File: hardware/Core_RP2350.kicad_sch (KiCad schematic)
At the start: 70 parts, among them SW1 SPST-NO, SW2 SPST-NO, SW3 SPST-NO, SW4 SPST-NO, SW5 SPST-NO, U1 RP2350B-QFN80, U2 LM4040A30IDBZR, U3 W25Q128JVS, U4 W25Q128JVS, U5 W25Q128JVS

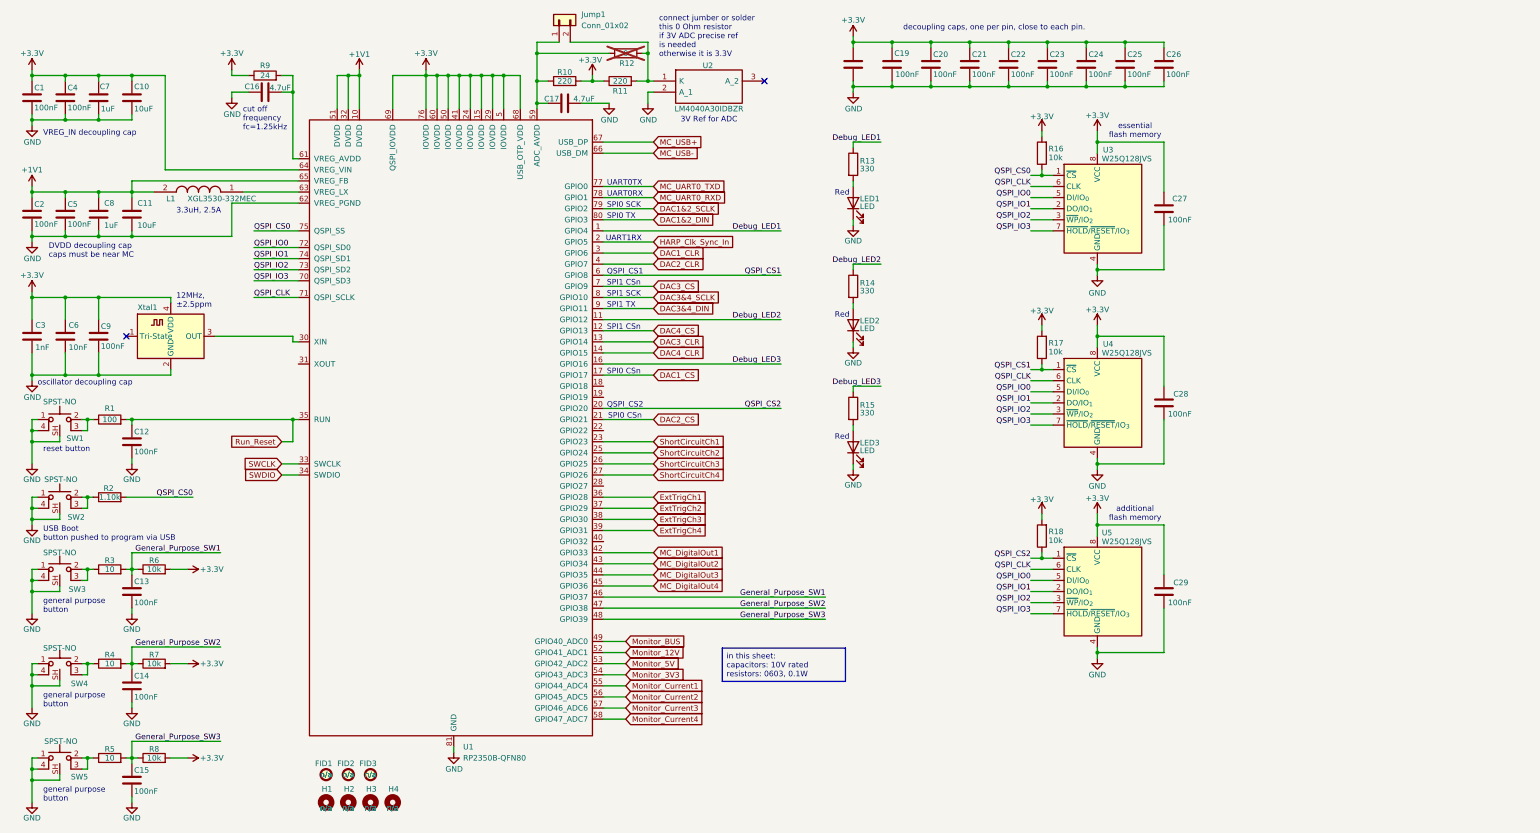
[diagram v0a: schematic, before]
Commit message: draft simplified rp2350 schematic w/sd card
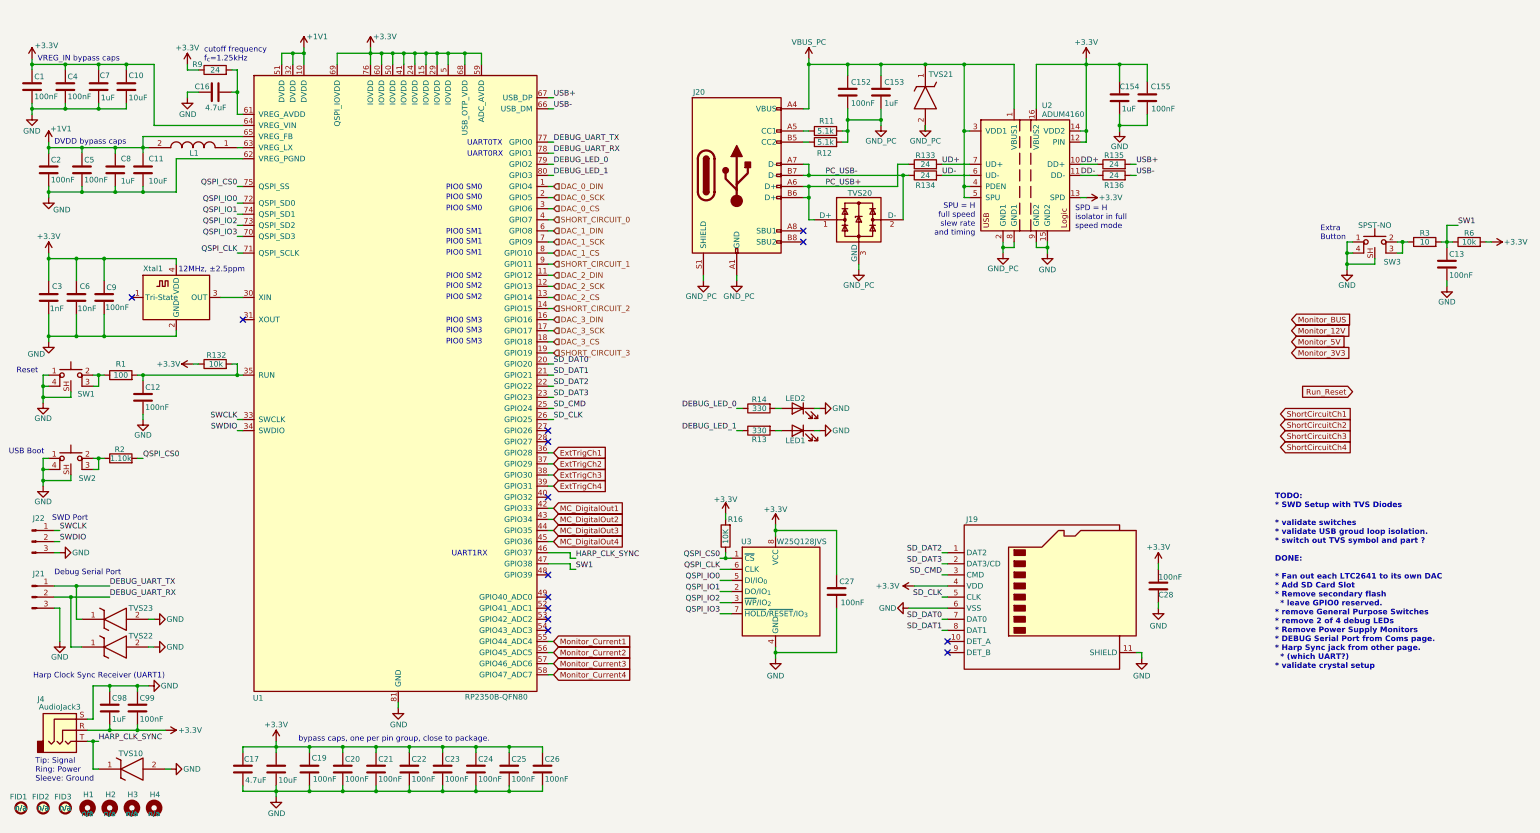
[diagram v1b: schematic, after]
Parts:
- removed C14, C15, C29: 100nF, Capacitor_SMD:C_0603_1608Metric, symbol harp.device.quad.dac:C_0603
- removed Jump1: Conn_01x02, Connector_PinHeader_2.54mm:PinHeader_1x02_P2.54mm_Vertical, symbol harp.device.quad.dac:Conn_01x02
- removed LED3: LED, harp.device.quad.dac.kicad:LED_0603_1608Metric_Pad1.05x0.95mm_HandSolder, symbol harp.device.quad.dac:LED
- removed R10: 220, Resistor_SMD:R_0603_1608Metric, symbol harp.device.quad.dac:R_0603
- removed R15: 330, Resistor_SMD:R_0603_1608Metric, symbol harp.device.quad.dac:R_0603
- removed R17, R18, R7, R8: 10k, Resistor_SMD:R_0603_1608Metric, symbol harp.device.quad.dac:R_0603
- removed R4, R5: 10, Resistor_SMD:R_0603_1608Metric, symbol harp.device.quad.dac:R_0603
- removed SW4, SW5: SPST-NO, harp.device.quad.dac.kicad:SW_Push_1P1T-SH_NO_Vertical_Wuerth_WS-TASV, symbol harp.device.quad.dac:SW_Push_with_gnd
- removed U2: LM4040A30IDBZR, harp.device.quad.dac.kicad:SOT95P237X112-3N, symbol harp.device.quad.dac:LM4040A30IDBZR
- removed U4, U5: W25Q128JVS, harp.device.quad.dac.kicad:SOIC-8_5.3x5.3mm_P1.27mm, symbol harp.device.quad.dac:W25Q128JVS
- added C152, C155, C99: 100nF, Capacitor_SMD:C_0603_1608Metric, symbol harp.device.quad.dac:C_0603
- added C153, C154, C98: 1uF, Capacitor_SMD:C_0603_1608Metric, symbol harp.device.quad.dac:C_0603
- added J19: Micro_SD_Card_Det_Hirose_DM3AT, Connector_Card:microSD_HC_Hirose_DM3AT-SF-PEJM5, symbol Connector:Micro_SD_Card_Det_Hirose_DM3AT
- added J20: USB_C_Receptacle_USB2.0, harp.device.quad.dac.kicad:USB_C_Receptacle_JAE_DX07S016JA1R1500, symbol harp.device.quad.dac:USB_C_Receptacle_USB2.0
- added J21, J22: 5-146281-3, harp.device.quad.dac.kicad:PinHeader_1x03_P2.54mm_Vertical, symbol harp.device.quad.dac:Conn_01x03_Male
- added J4: AudioJack3, harp.device.quad.dac.kicad:Jack_3.5mm_CUI_SJ-3524-SMT_Horizontal, symbol harp.device.quad.dac:AudioJack3
- added R132: 10k, Resistor_SMD:R_0603_1608Metric, symbol harp.device.quad.dac:R_0603
- added R133, R134, R135, R136: 24, Resistor_SMD:R_0603_1608Metric, symbol harp.device.quad.dac:R_0603
- added TVS10, TVS21, TVS22, TVS23: ESD441DPLR, harp.device.quad.dac.kicad:ESD441DPLR, symbol harp.device.quad.dac:ESD441DPLR
- added TVS20: TPD2EUSB30, Package_TO_SOT_SMD:Texas_DRT-3, symbol harp.device.quad.dac:TPD2EUSB30
- added U2: ADUM4160, harp.device.quad.dac.kicad:SOIC-16W_7.5x10.3mm_P1.27mm, symbol harp.device.quad.dac:ADUM4160
- R11: value 220 -> 5.1k; Link https://www.digikey.com/en/products/detail/yageo/RC0603FR-07220RL/727061 -> https://www.digikey.com/en/products/detail/yageo/RC0603FR-075K1L/727268; Manufacturer Number RT0402BRD071KL -> RT0402FRE075K1L; Manufacturer_Part_Number RC0603FR-07220RL -> RC0603FR-075K1L; PCBWay Link (none) -> https://www.pcbway.com/components/detail/RT0402FRE075K1L/44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
- R12: value 0 -> 5.1k; Link https://www.digikey.com/en/products/detail/yageo/RC0603JR-0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 -> https://www.digikey.com/en/products/detail/yageo/RC0603FR-0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; Manufacturer Number RT0402BRD071KL -> RT0402FRE075K1L; Manufacturer_Part_Number RC0603JR-070RL -> RC0603FR-075K1L; PCBWay Link (none) -> https://www.pcbway.com/components/detail/RT0402FRE075K1L/44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; Tolerance (none) -> 1%; now fitted; now in the parts list
- R16: value 10k -> 10K
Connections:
- net General_Purpose_SW2 is gone; now on net SW1: U1.47 (GPIO38)
- net +3.3V: now also C17.1, C28.1, U1.59 (ADC_AVDD), C154.1, C155.2, C98.2, C99.1, J19.4 (VDD), J4.R, R132.1, U2.12 (PIN), U2.13 (SPD), U2.14 (VDD2), U2.16 (VBUS2); no longer C28.2, R11.1
- net GND: now also C28.2, C154.2, C155.1, C98.1, C99.2, J19.11 (SHIELD), J19.6 (VSS), J21.3 (Pin_3), J22.3 (Pin_3), J4.S, TVS10.2, TVS22.2, TVS23.2, U2.15 (GND2), U2.9 (GND2); no longer C28.1
- net Monitor_12V: no longer U1.52 (GPIO41_ADC1)
- net Monitor_3V3: no longer U1.54 (GPIO43_ADC3)
- net Monitor_5V: no longer U1.53 (GPIO42_ADC2)
- net Monitor_BUS: no longer U1.49 (GPIO40_ADC0)
- net Run_Reset: no longer C12.2, R1.2, U1.35 (RUN)
- net SWCLK: now also J22.1 (Pin_1)
- net SWDIO: now also J22.2 (Pin_2)
- net ShortCircuitCh1: no longer U1.23 (GPIO23)
- net ShortCircuitCh2: no longer U1.25 (GPIO24)
- net ShortCircuitCh3: no longer U1.26 (GPIO25)
- net ShortCircuitCh4: no longer U1.27 (GPIO26)
- net GND_PC: now reaches R11.2, R12.2
- net GND_PC: now also C152.1, C153.2, J20.A1 (GND), J20.A12 (GND), J20.B1 (GND), J20.B12 (GND), J20.S1 (SHIELD), TVS20.3 (GND), TVS21.2, U2.2 (GND1), U2.8 (GND1)
- net DAC_3_CS: now reaches U1.18 (GPIO18)
- net SHORT_CIRCUIT_3: now reaches U1.19 (GPIO19)
- net SD_DAT2: now reaches U1.22 (GPIO22)
- net SD_DAT2: now also J19.1 (DAT2)
- net DAC1&2_DIN renamed DEBUG_LED_1
- net DEBUG_LED_1: now also R13.1
- net DAC1&2_SCLK renamed DEBUG_LED_0
- net DEBUG_LED_0: now also R14.1
- net DAC1_CLR renamed DAC_0_CS
- net DAC1_CS renamed DAC_3_SCK
- net DAC2_CLR renamed SHORT_CIRCUIT_0
- net DAC2_CS renamed SD_DAT1
- net SD_DAT1: now also J19.8 (DAT1)
- net DAC3&4_DIN renamed SHORT_CIRCUIT_1
- net DAC3&4_SCLK renamed DAC_1_CS
- net DAC3_CLR renamed DAC_2_CS
- net DAC3_CS renamed DAC_1_SCK
- net DAC4_CLR renamed SHORT_CIRCUIT_2
- net DAC4_CS renamed DAC_2_SCK
- net Debug_LED1 renamed DAC_0_DIN
- net DAC_0_DIN: no longer R13.1
- net Debug_LED2 renamed DAC_2_DIN
- net DAC_2_DIN: no longer R14.1
- net Debug_LED3 renamed DAC_3_DIN
- net General_Purpose_SW1 renamed SW1
- net SW1: no longer U1.46 (GPIO37)
- net General_Purpose_SW3: no longer names the net of U1.48 (GPIO39)
- net HARP_Clk_Sync_In renamed DAC_0_SCK
- net MC_UART0_RXD renamed DEBUG_UART_RX
- net DEBUG_UART_RX: now also J21.2 (Pin_2), TVS22.1
- net MC_UART0_TXD renamed DEBUG_UART_TX
- net DEBUG_UART_TX: now also J21.1 (Pin_1), TVS23.1
- net MC_USB+ renamed USB+
- net USB+: now also R135.2
- net MC_USB- renamed USB-
- net USB-: now also R136.2
- net QSPI_CS1 renamed DAC_1_DIN
- net QSPI_CS2 renamed SD_DAT0
- net SD_DAT0: now also J19.7 (DAT0)
- new net: C12.2, R1.2, R132.2, U1.35 (RUN)
- new net: J20.A5 (CC1), R11.1
- new net: J20.B5 (CC2), R12.1
- new net DD+: R135.1, U2.10 (DD+)
- new net DD-: R136.1, U2.11 (DD-)
- new net HARP_CLK_SYNC: J4.T, TVS10.1, U1.46 (GPIO37)
- new net PC_USB+: J20.A6 (D+), J20.B6 (D+), R133.1, TVS20.1 (D+)
- new net PC_USB-: J20.A7 (D-), J20.B7 (D-), R134.1, TVS20.2 (D-)
- new net SD_CLK: J19.5 (CLK), U1.26 (GPIO25)
- new net SD_CMD: J19.3 (CMD), U1.25 (GPIO24)
- new net SD_DAT3: J19.2 (DAT3/CD), U1.23 (GPIO23)
- new net UD+: R133.2, U2.7 (UD+)
- new net UD-: R134.2, U2.6 (UD-)
- new net VBUS_PC: C152.2, C153.1, J20.A4 (VBUS), J20.A9 (VBUS), J20.B4 (VBUS), J20.B9 (VBUS), TVS21.1, U2.1 (VBUS1), U2.3 (VDD1), U2.4 (PDEN), U2.5 (SPU)
- no-connect marks 2 -> 14
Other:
- note added: "DVDD bypass caps"
- note added: "Debug Serial Port"
- note added: "Extra Button"
- note added: "Harp Clock Sync Receiver (UART1)"
- note added: "PIO0 SM0"
- note added: "PIO0 SM1"
- note added: "PIO0 SM2"
- note added: "PIO0 SM3"
- note added: "Reset"
- note added: "SPD = H isolator in full speed mode"
- note added: "SPU = H full speed slew rate and timing"
- note added: "SWD Port"
- note added: "TODO: * SWD Setup with TVS Diodes * validate switches * validate USB groud loop isolation. * switch out TVS symbol and part ? DONE: * Fan out each LTC2641 to its own DAC * Add SD Card Slot * Remove secondary flash * leave GPIO0 reserved. * remove General Purpose Switches * remove 2 of 4 debug LEDs * Remove Power Supply Monitors * DEBUG Serial Port from Coms page. * Harp Sync jack from other page.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"
- note added: "Tip: Signal Ring: Power Sleeve: Ground"
- note added: "USB Boot"
- note added: "VREG_IN bypass caps"
- note added: "bypass caps, one per pin group, close to package."
- note added: "cutoff frequency f_{c}=1.25kHz"
- note removed: "3.3uH, 2.5A"
- note removed: "3V Ref for ADC"
- note removed: "DVDD decoupling cap caps must be near MC"
- note removed: "QSPI_CS1"
- note removed: "QSPI_CS2"
- note removed: "Red"
- note removed: "SPI0 CSn"
- note removed: "SPI0 SCK"
- note removed: "SPI0 TX"
- note removed: "SPI1 CSn"
- note removed: "SPI1 SCK"
- note removed: "SPI1 TX"
- note removed: "USB Boot button pushed to program via USB"
- note removed: "VREG_IN decoupling cap"
- note removed: "additional flash memory"
- note removed: "connect jumber or solder this 0 Ohm resistor if 3V ADC precise ref is needed otherwise it is 3.3V"
- note removed: "cut off frequency fc=1.25kHz"
- note removed: "decoupling caps, one per pin, close to each pin."
- note removed: "essential flash memory"
- note removed: "general purpose button"
- note removed: "oscillator decoupling cap"
- note removed: "reset button"
- moved on the sheet: C1, C10, C11, C12, C13, C16, C17, C19, C2, C20, C21, C22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

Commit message: draft new analog signal chain & short-circuit detection
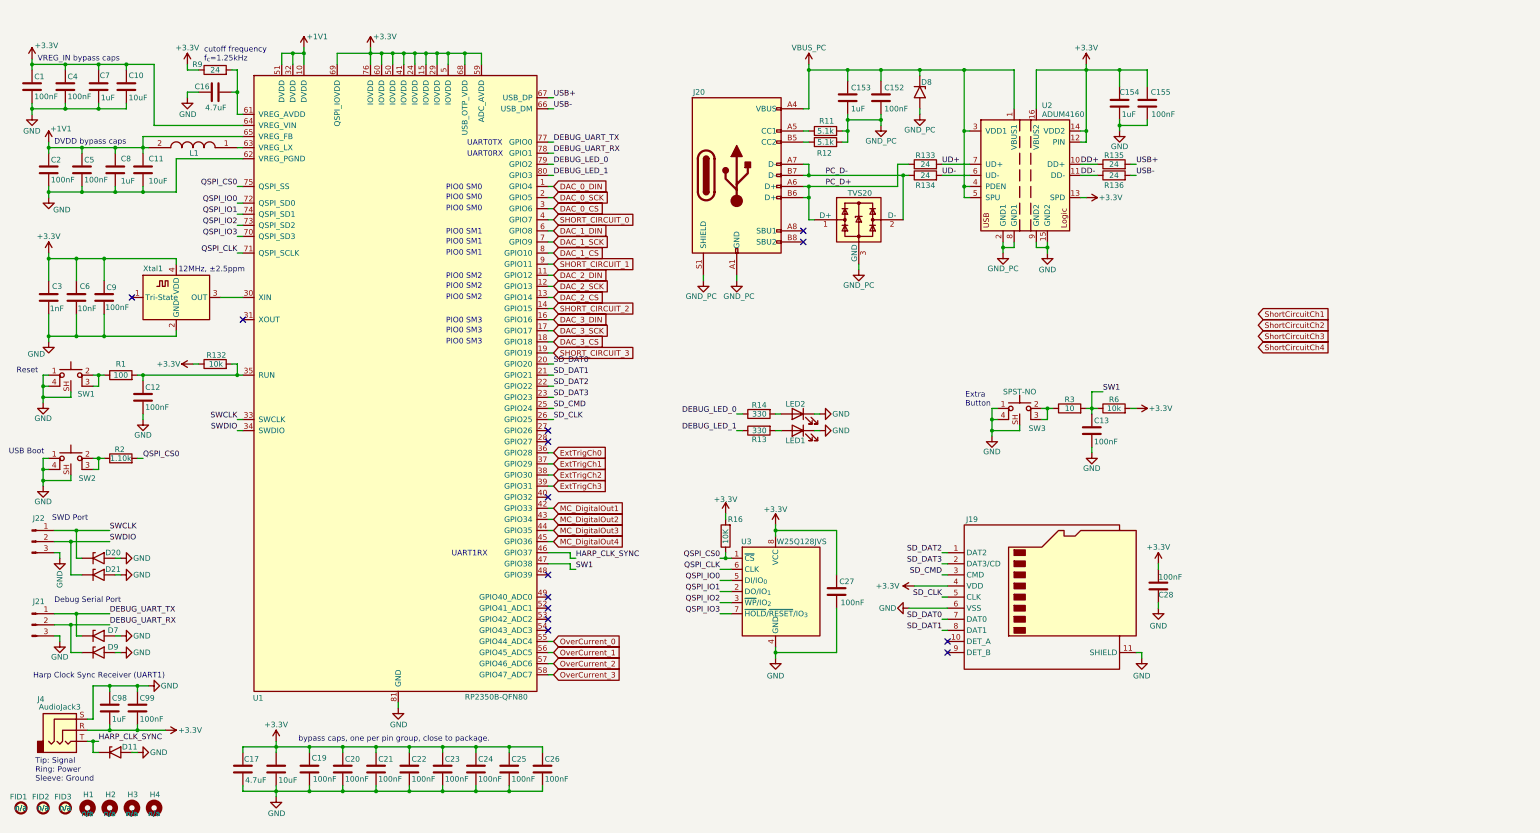
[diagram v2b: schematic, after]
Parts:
- removed TVS10, TVS21, TVS22, TVS23: ESD441DPLR, harp.device.quad.dac.kicad:ESD441DPLR, symbol harp.device.quad.dac:ESD441DPLR
- added D11, D20, D21, D7, D8, D9: VBUS05N1-HD1-G3-08, Diode_SMD:D_SOD-882, symbol kicad_component_library:VBUS05N1-HD1-G3-08
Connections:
- net ExtTrigCh4 is gone; now on net ExtTrigCh3: U1.39 (GPIO31)
- net DEBUG_UART_RX: now also D9.1 (A1)
- net DEBUG_UART_TX: now also D7.1 (A1)
- net ExtTrigCh1: now also U1.37 (GPIO29); no longer U1.36 (GPIO28)
- net ExtTrigCh2: now also U1.38 (GPIO30); no longer U1.37 (GPIO29)
- net ExtTrigCh3: no longer U1.38 (GPIO30)
- net GND: now also D11.2 (A2), D20.2 (A2), D21.2 (A2), D7.2 (A2), D9.2 (A2)
- net GND_PC: now also D8.2 (A2)
- net HARP_CLK_SYNC: now also D11.1 (A1)
- net SWCLK: now also D20.1 (A1)
- net SWDIO: now also D21.1 (A1)
- net VBUS_PC: now also D8.1 (A1)
- net Monitor_Current1 renamed OverCurrent_0
- net Monitor_Current2 renamed OverCurrent_1
- net Monitor_Current3 renamed OverCurrent_2
- net Monitor_Current4 renamed OverCurrent_3
- net PC_USB+ renamed PC_D+
- net PC_USB- renamed PC_D-
- new net ExtTrigCh0: U1.36 (GPIO28)
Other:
- note removed: "SPD = H isolator in full speed mode"
- note removed: "SPU = H full speed slew rate and timing"
- note removed: "TODO: * SWD Setup with TVS Diodes * validate switches * validate USB groud loop isolation. * switch out TVS symbol and part ? DONE: * Fan out each LTC2641 to its own DAC * Add SD Card Slot * Remove secondary flash * leave GPIO0 reserved. * remove General Purpose Switches * remove 2 of 4 debug LEDs * Remove Power Supply Monitors * DEBUG Serial Port from Coms page. * Harp Sync jack from other page.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"
- moved on the sheet: C13, C152, C153, C154, C155, J21, LED2, R14, R3, R6, SW3

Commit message: draft split rail power supply design
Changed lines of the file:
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@@
-		)
-	)
-	(global_label "ShortCircuitCh1"
-		(shape input)
-		(at 299.72 81.28 0)
-		(fields_autoplaced yes)
-		(effects
-			(font
-				(size 1.27 1.27)
-			)
-			(justify left)
-		)
-		(property "Intersheetrefs" "${INTERSHEET_REFS}"
-			(at 317.5822 81.28 0)
-			(effects
-				(font
-					(size 1.27 1.27)
-				)
-				(justify left)
-				(hide yes)
-			)
 		)
 	)
@@
 		)
 	)
-	(global_label "ShortCircuitCh3"
-		(shape input)
-		(at 299.72 86.36 0)
-		(fields_autoplaced yes)
-		(effects
-			(font
-				(size 1.27 1.27)
-			)
-			(justify left)
-		)
-		(property "Intersheetrefs" "${INTERSHEET_REFS}"
-			(at 317.5822 86.36 0)
-			(effects
-				(font
-					(size 1.27 1.27)
-				)
-				(justify left)
-				(hide yes)
-			)
-		)
-	)
-	(global_label "ShortCircuitCh4"
-		(shape input)
-		(at 299.72 88.9 0)
-		(fields_autoplaced yes)
-		(effects
-			(font
-				(size 1.27 1.27)
-			)
-			(justify left)
-		)
-		(property "Intersheetrefs" "${INTERSHEET_REFS}"
-			(at 317.5822 88.9 0)
-			(effects
-				(font
-					(size 1.27 1.27)
-				)
-				(justify left)
-				(hide yes)
-			)
-		)
-	)
 	(global_label "DAC_2_CS"
 		(shape input)
@@
 			(effects
 				(font
-					(size 1.27 1.27)
-				)
-				(justify left)
-				(hide yes)
-			)
-		)
-	)
-	(global_label "ShortCircuitCh2"
-		(shape input)
-		(at 299.72 83.82 0)
-		(fields_autoplaced yes)
-		(effects
-			(font
-				(size 1.27 1.27)
-			)
-			(justify left)
-		)
-		(property "Intersheetrefs" "${INTERSHEET_REFS}"
-			(at 317.5822 83.82 0)
-			(effects
-				(font
